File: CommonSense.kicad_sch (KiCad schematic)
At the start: 31 parts, among them J1 Conn_02x04_Counter_Clockwise, U1 NRF52810-QFAA-R7, U2 SHT41-AD1B-R2, Y1 ECS-.327-12.5-12R-TR, Y2 ABM11W-32.0000MHZ-7-D1X-T3

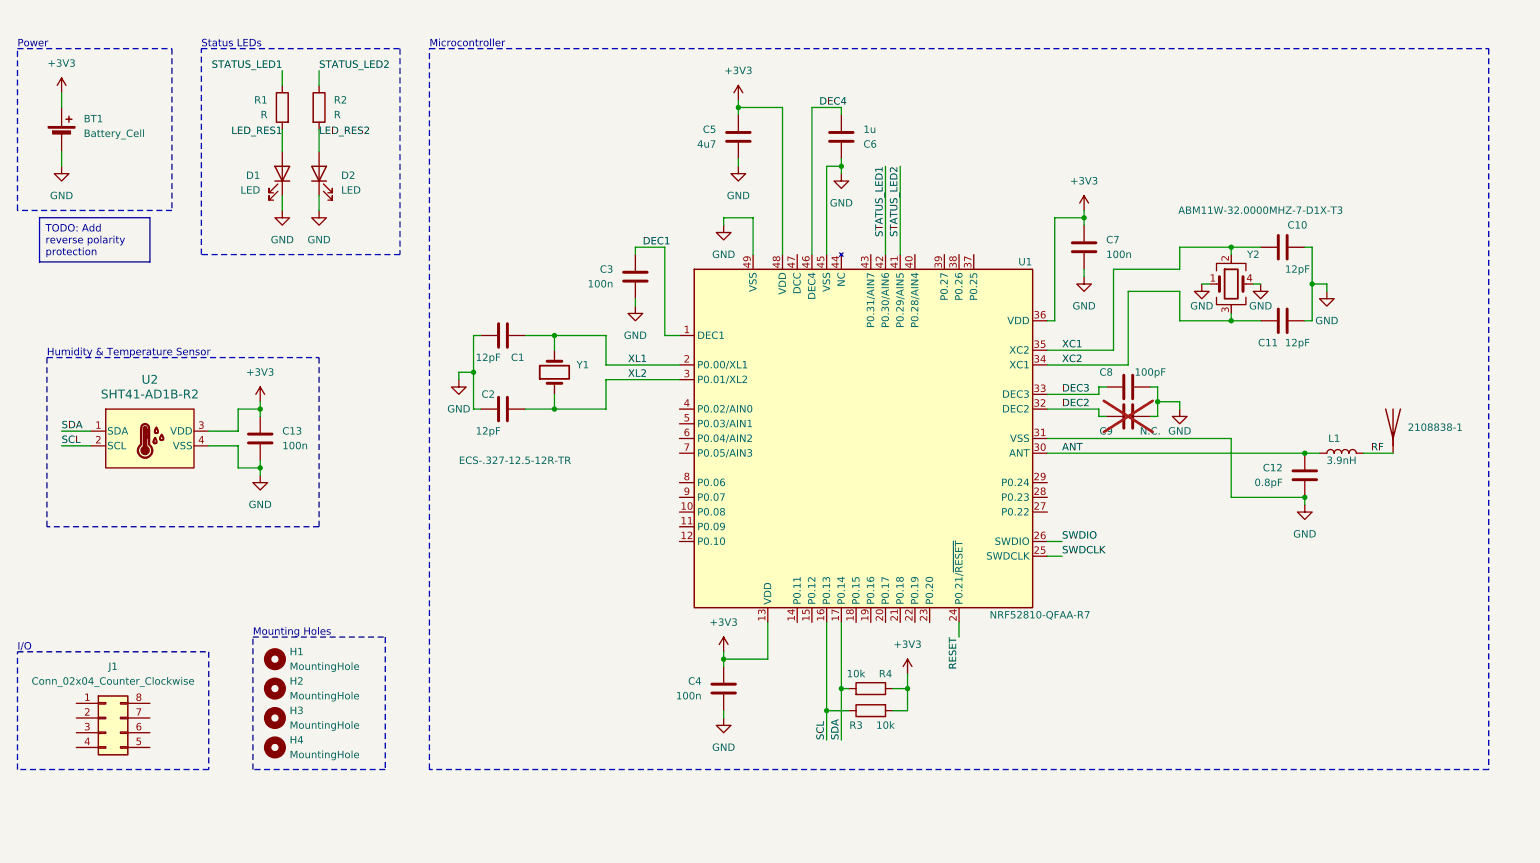
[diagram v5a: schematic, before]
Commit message: Connect IOs and AINs to pin header
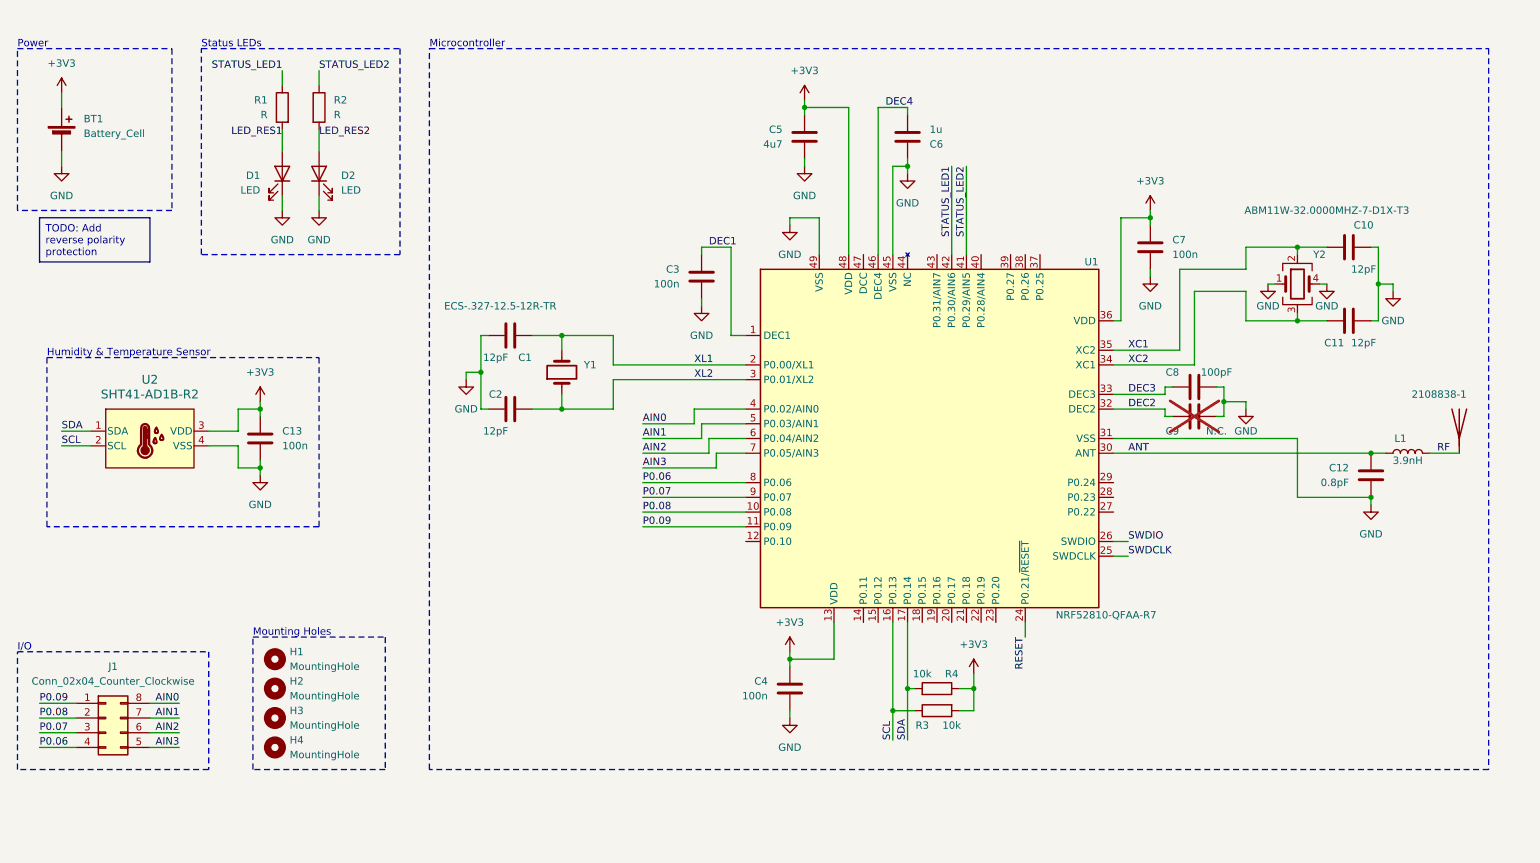
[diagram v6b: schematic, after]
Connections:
- net P0.08: now reaches U1.10 (P0.08)
- net P0.08: now also J1.2 (Pin_2)
- net P0.09: now reaches U1.11 (P0.09)
- net P0.09: now also J1.1 (Pin_1)
- net AIN0: now reaches U1.4 (P0.02/AIN0)
- net AIN0: now also J1.8 (Pin_8)
- net AIN1: now reaches U1.5 (P0.03/AIN1)
- net AIN1: now also J1.7 (Pin_7)
- net AIN2: now reaches U1.6 (P0.04/AIN2)
- net AIN2: now also J1.6 (Pin_6)
- net AIN3: now reaches U1.7 (P0.05/AIN3)
- net AIN3: now also J1.5 (Pin_5)
- net P0.06: now reaches U1.8 (P0.06)
- net P0.06: now also J1.4 (Pin_4)
- net P0.07: now reaches U1.9 (P0.07)
- net P0.07: now also J1.3 (Pin_3)
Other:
- moved on the sheet: 2108838-1, C1, C10, C11, C12, C2, C3, C4, C5, C6, C7, C8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

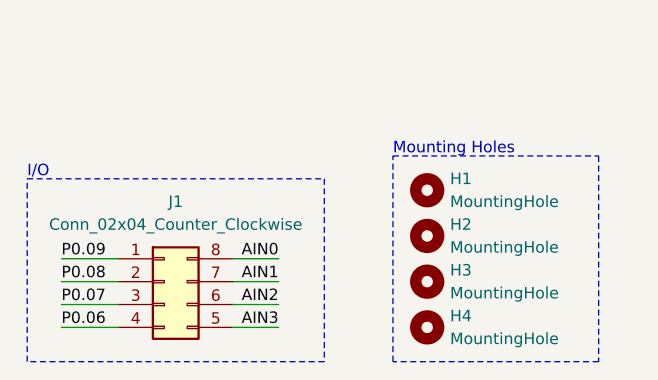
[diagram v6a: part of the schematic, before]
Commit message: Finish routing ADC in IO pins
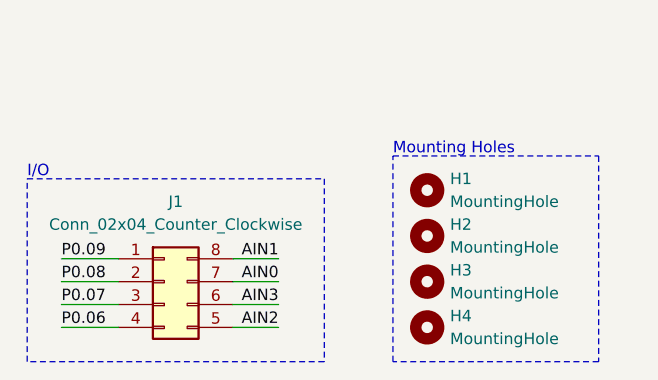
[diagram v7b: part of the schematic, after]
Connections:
- net AIN0: now also J1.7 (Pin_7); no longer J1.8 (Pin_8)
- net AIN1: now also J1.8 (Pin_8); no longer J1.7 (Pin_7)
- net AIN2: now also J1.5 (Pin_5); no longer J1.6 (Pin_6)
- net AIN3: now also J1.6 (Pin_6); no longer J1.5 (Pin_5)
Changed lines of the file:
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@@
     (effects (font (size 1.27 1.27)) (justify left bottom))
+  )
+  (label "AIN2" (at 49.53 153.67 180) (fields_autoplaced)
+    (effects (font (size 1.27 1.27)) (justify right bottom))
   )
   (label "SWDIO" (at 213.36 118.11 0) (fields_autoplaced)
@@
     (effects (font (size 1.27 1.27)) (justify right bottom))
   )
-  (label "AIN1" (at 49.53 148.59 180) (fields_autoplaced)
-    (effects (font (size 1.27 1.27)) (justify right bottom))
-  )
   (label "XL2" (at 138.43 90.17 0) (fields_autoplaced)
     (effects (font (size 1.27 1.27)) (justify left bottom))
@@
     (effects (font (size 1.27 1.27)) (justify left bottom))
   )
-  (label "AIN3" (at 49.53 153.67 180) (fields_autoplaced)
-    (effects (font (size 1.27 1.27)) (justify right bottom))
-  )
   (label "DEC2" (at 213.36 95.25 0) (fields_autoplaced)
     (effects (font (size 1.27 1.27)) (justify left bottom))
@@
   (label "P0.08" (at 25.4 148.59 0) (fields_autoplaced)
     (effects (font (size 1.27 1.27)) (justify left bottom))
+  )
+  (label "AIN3" (at 49.53 151.13 180) (fields_autoplaced)
+    (effects (font (size 1.27 1.27)) (justify right bottom))
   )
   (label "LED_RES1" (at 67.31 48.26 180) (fields_autoplaced)
@@
     (effects (font (size 1.27 1.27)) (justify left bottom))
   )
+  (label "AIN1" (at 49.53 146.05 180) (fields_autoplaced)
+    (effects (font (size 1.27 1.27)) (justify right bottom))
+  )
   (label "SWDCLK" (at 213.36 120.65 0) (fields_autoplaced)
     (effects (font (size 1.27 1.27)) (justify left bottom))
@@
   (label "DEC4" (at 171.45 43.18 0) (fields_autoplaced)
     (effects (font (size 1.27 1.27)) (justify left bottom))
-  )
-  (label "AIN0" (at 49.53 146.05 180) (fields_autoplaced)
-    (effects (font (size 1.27 1.27)) (justify right bottom))
   )
   (label "XL1" (at 138.43 87.63 0) (fields_autoplaced)
@@
     (effects (font (size 1.27 1.27)) (justify right bottom))
   )
-  (label "AIN2" (at 49.53 151.13 180) (fields_autoplaced)
+  (label "AIN0" (at 49.53 148.59 180) (fields_autoplaced)
     (effects (font (size 1.27 1.27)) (justify right bottom))
   )
